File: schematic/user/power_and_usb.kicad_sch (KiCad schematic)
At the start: 40 parts, among them J1 TYPE-C-31-M-04, Q1 AO3401A, Q2 AO3401A, Q5 MBT3904DW1T1, U1 TP4056, U2 MAX17048G+T10, U3 NCP167AFCT330T2G, U6 ESD122DMXR, U7 WUSB3801

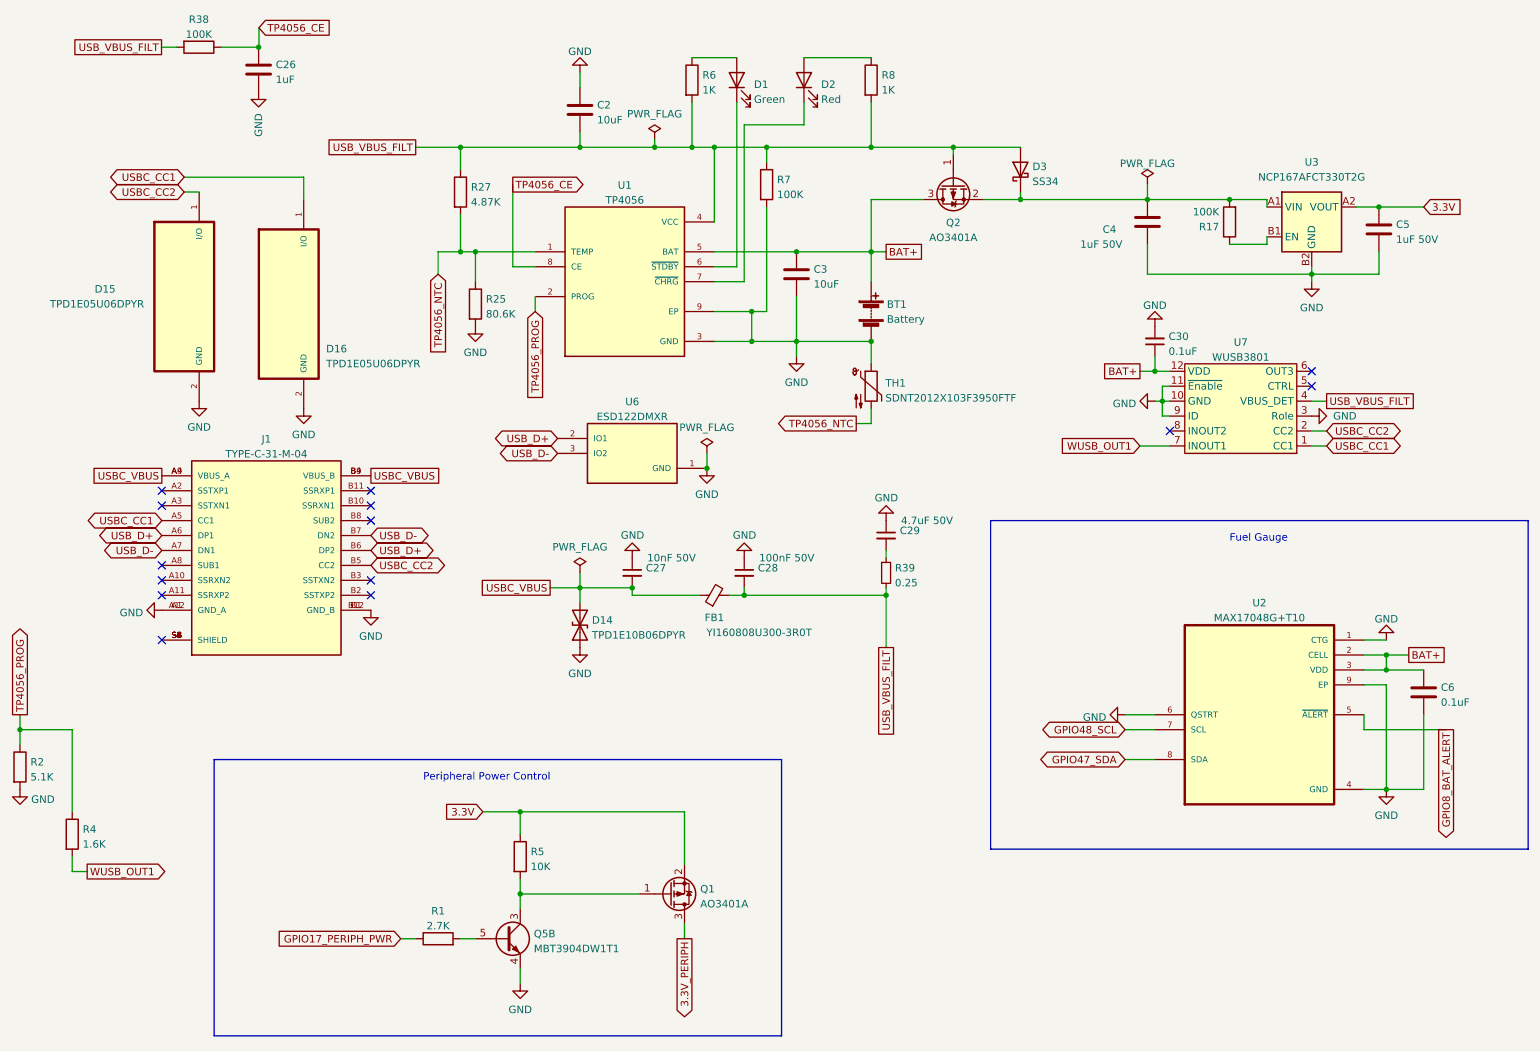
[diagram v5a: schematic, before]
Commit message: v0.7 board: optimize component selection for USB input filter.
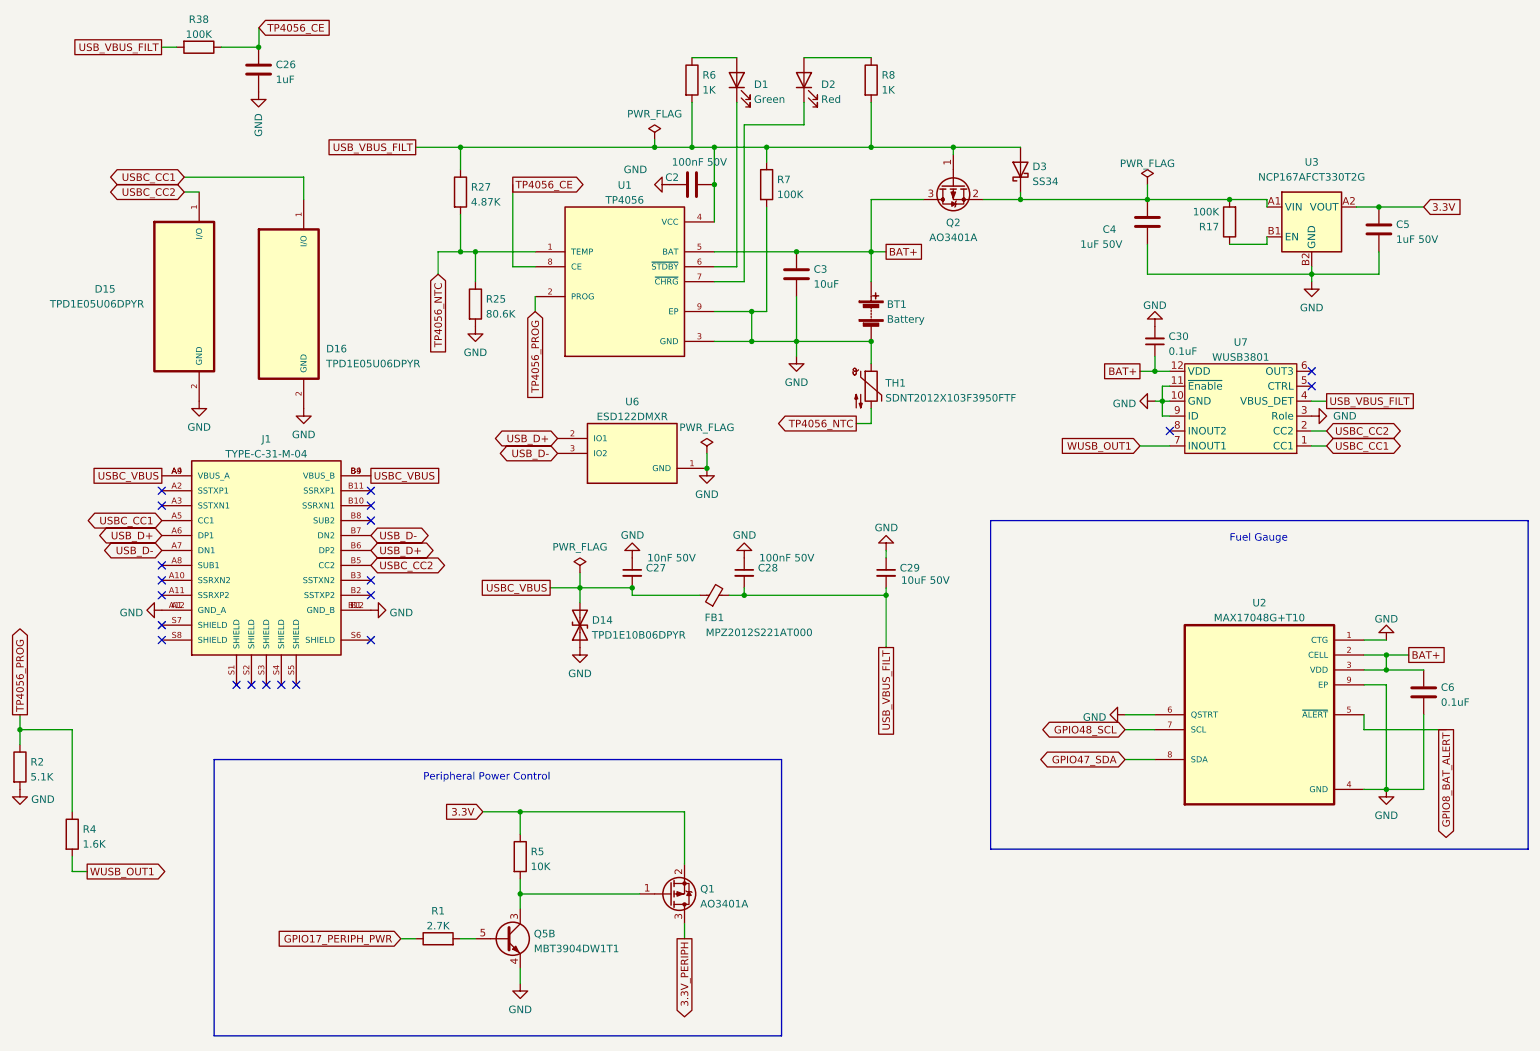
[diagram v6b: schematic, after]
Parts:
- removed R39: 0.25, Resistor_SMD:R_0603_1608Metric, symbol Device:R_Small
- C2: value 10uF -> 100nF 50V; LCSC C315248 -> C307331
- C29: value 4.7uF 50V -> 10uF 50V; LCSC C412634 -> C440198
- FB1: value YI160808U300-3R0T -> MPZ2012S221AT000; footprint Inductor_SMD:L_0603_1608Metric -> Inductor_SMD:L_0805_2012Metric; LCSC C3011213 -> C76818
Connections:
- net USB_VBUS_FILT: now also C29.2
- now unconnected: J1.S1 (SHIELD), J1.S2 (SHIELD), J1.S3 (SHIELD), J1.S4 (SHIELD), J1.S5 (SHIELD), J1.S6 (SHIELD), J1.S7 (SHIELD), J1.S8 (SHIELD)
- no-connect marks 14 -> 21
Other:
- moved on the sheet: C2, C29

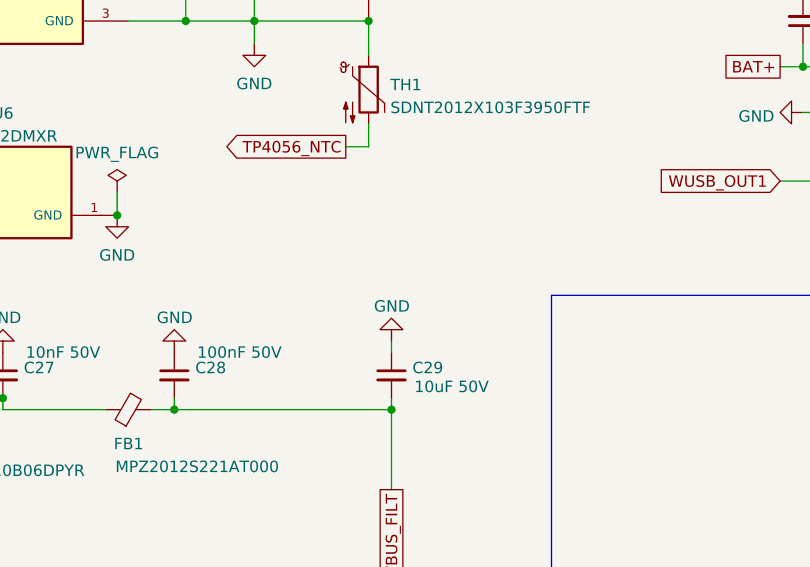
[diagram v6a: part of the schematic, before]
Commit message: v0.7 board: add 2 ohm series resistance to dampen resonance.
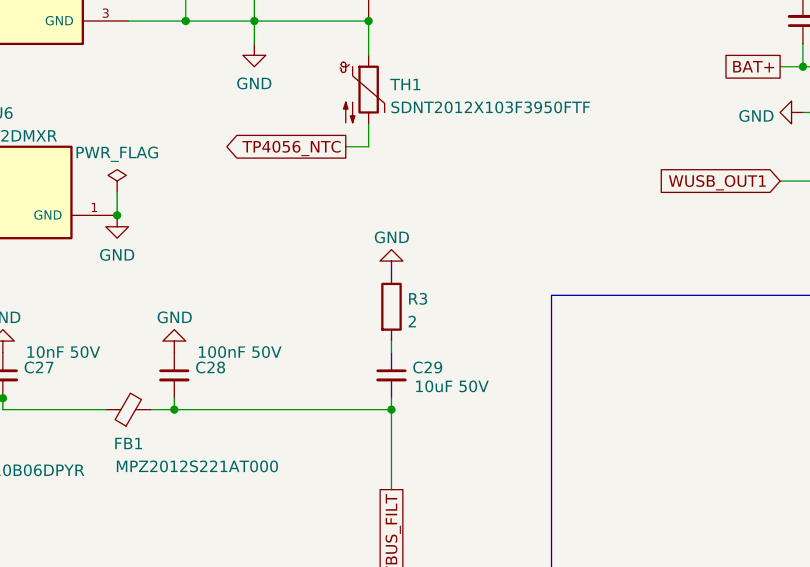
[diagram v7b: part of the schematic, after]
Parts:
- added R3: 2, Resistor_SMD:R_0402_1005Metric, symbol Device:R
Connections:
- net GND: now also R3.1; no longer C29.1
- new net: C29.1, R3.2
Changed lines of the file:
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@@
     (pin "1")
+  )
+  (symbol (lib_id "Device:R") (at 168.91 100.33 0) (unit 1)
+    (in_bom yes) (on_board yes) (fields_autoplaced)
+    (property "Reference" "R3" (id 0) (at 170.688 99.4953 0)
+      (effects (font (size 1.27 1.27)) (justify left))
+    )
+    (property "Value" "2" (id 1) (at 170.688 102.0322 0)
+      (effects (font (size 1.27 1.27)) (justify left))
+    )
+    (property "Footprint" "Resistor_SMD:R_0402_1005Metric" (id 2) (at 167.132 100.33 90)
+      (effects (font (size 1.27 1.27)) hide)
+    )
+    (property "Datasheet" "https://datasheet.lcsc.com/lcsc/2205312300_UNI-ROYAL-Uniroyal-Elec-0402WGF200KTCE_C270630.pdf" (id 3) (at 168.91 100.33 0)
+      (effects (font (size 1.27 1.27)) hide)
+    )
+    (property "LCSC" "C270630" (id 4) (at 168.91 100.33 0)
+      (effects (font (size 1.27 1.27)) hide)
+    )
+    (pin "1")
+    (pin "2")
   )
   (symbol (lib_id "Device:R") (at 227.33 48.26 180) (unit 1)
@@
     (pin "2")
   )
-  (symbol (lib_id "power:GND") (at 168.91 104.14 180) (unit 1)
-    (in_bom yes) (on_board yes)
-    (property "Reference" "#PWR057" (id 0) (at 168.91 97.79 0)
-      (effects (font (size 1.27 1.27)) hide)
-    )
-    (property "Value" "GND" (id 1) (at 166.9601 100.2819 0)
+  (symbol (lib_id "power:GND") (at 168.91 96.52 180) (unit 1)
+    (in_bom yes) (on_board yes)
+    (property "Reference" "#PWR057" (id 0) (at 168.91 90.17 0)
+      (effects (font (size 1.27 1.27)) hide)
+    )
+    (property "Value" "GND" (id 1) (at 166.9601 92.6619 0)
       (effects (font (size 1.27 1.27)) (justify right))
     )
-    (property "Footprint" "" (id 2) (at 168.91 104.14 0)
-      (effects (font (size 1.27 1.27)) hide)
-    )
-    (property "Datasheet" "" (id 3) (at 168.91 104.14 0)
-      (effects (font (size 1.27 1.27)) hide)
-    )
+    (property "Footprint" "" (id 2) (at 168.91 96.52 0)
+      (effects (font (size 1.27 1.27)) hide)
+    )
+    (property "Datasheet" "" (id 3) (at 168.91 96.52 0)
+      (effects (font (size 1.27 1.27)) hide)
+    )

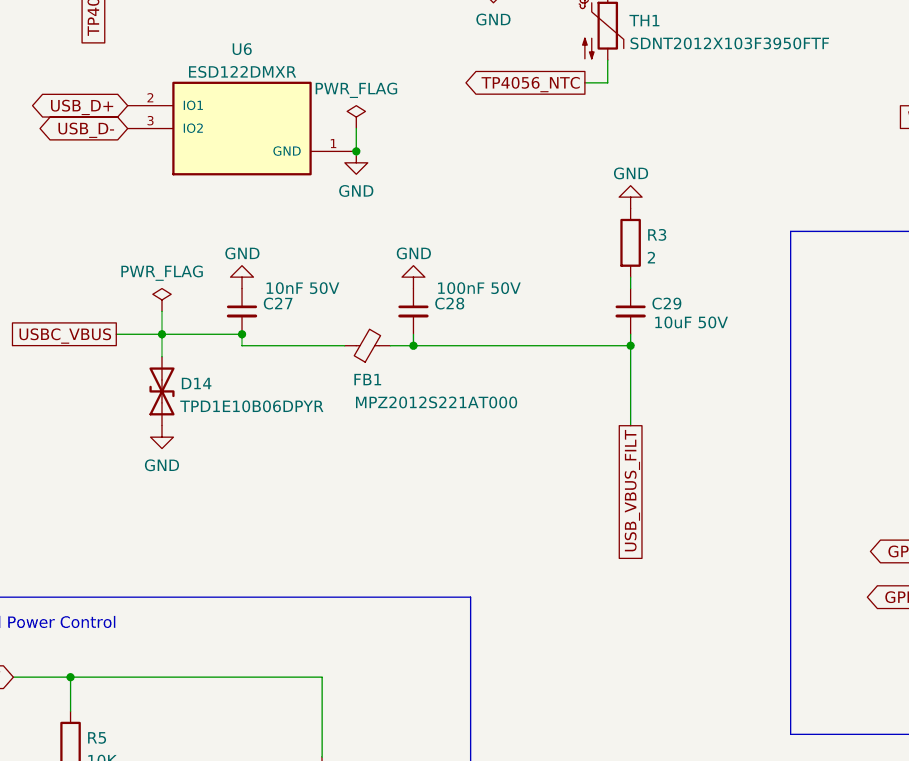
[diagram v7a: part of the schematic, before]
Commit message: v0.7 board:
1. Undo addition of USB filter as LDO is able to block noise/ripple from it.
2. Tweak LDO footprint and traces leading from it based on https://www.onsemi.jp/pub/Collateral/AN-5075.PDF (to improve yield).
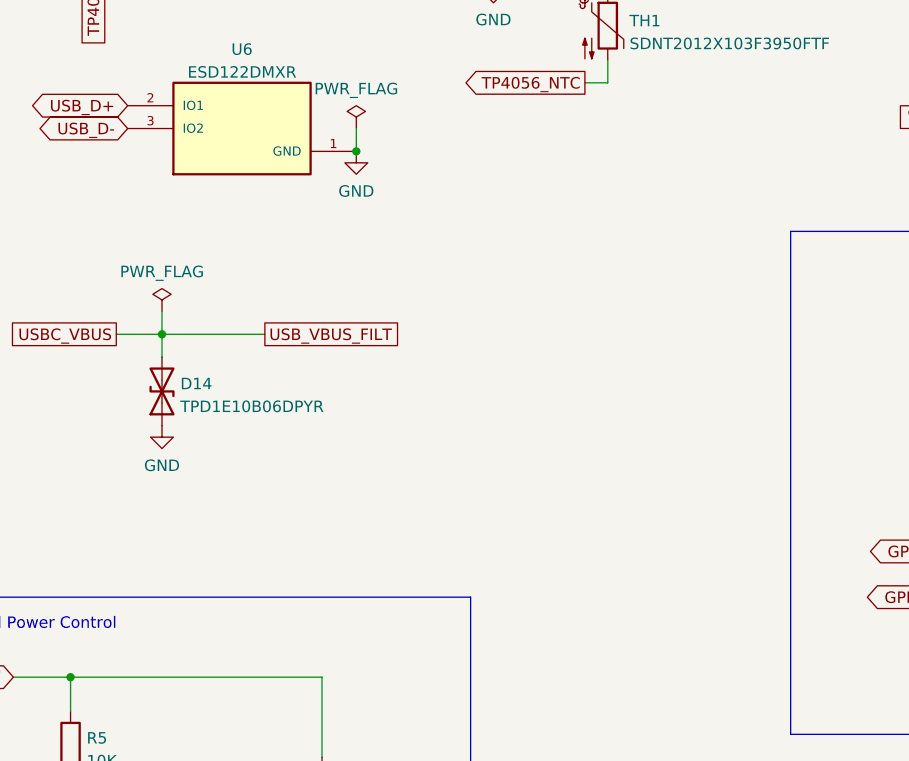
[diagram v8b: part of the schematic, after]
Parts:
- removed C27: 10nF 50V, Capacitor_SMD:C_0402_1005Metric, symbol Device:C_Small
- removed C28: 100nF 50V, Capacitor_SMD:C_0402_1005Metric, symbol Device:C_Small
- removed C29: 10uF 50V, Capacitor_SMD:C_0805_2012Metric, symbol Device:C_Small
- removed FB1: MPZ2012S221AT000, Inductor_SMD:L_0805_2012Metric, symbol Device:FerriteBead_Small
- removed R3: 2, Resistor_SMD:R_0402_1005Metric, symbol Device:R
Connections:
- net USB_VBUS_FILT is gone; now on net USBC_VBUS: C2.2, D3.2 (A), Q2.1 (G), R27.1, R38.2, R6.2, R7.1, R8.2, U1.4 (VCC), U7.4 (VBUS_DET)
